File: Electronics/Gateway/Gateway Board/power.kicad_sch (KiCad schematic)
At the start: 25 parts, among them IC201 TPS54295PWPR, J2 Screw_Terminal_01x02, J202 Conn_01x02_Pin, J203 Conn_01x02_Pin, J204 Conn_01x02_Pin

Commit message: Schematic updates
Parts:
- removed C10, C11: 10n, Capacitor_SMD:C_0402_1005Metric, symbol Device:C_Small
- removed C3, C4: 100n, Capacitor_SMD:C_0402_1005Metric, symbol Device:C_Small
- removed C5: 1u, Capacitor_SMD:C_0402_1005Metric, symbol Device:C_Small
- removed C6, C7: 47u, Capacitor_SMD:C_0805_2012Metric, symbol Device:C_Small
- removed C8, C9: 10u, Capacitor_SMD:C_0603_1608Metric, symbol Device:C_Small
- removed D1: BAT760-115, Diode_SMD:D_SOD-323, symbol Device:D_Schottky
- removed D2, D3: Green, LED_SMD:LED_0603_1608Metric, symbol Device:LED_Small
- removed IC201: TPS54295PWPR, SOP65P640X120-17N, symbol TPS54295PWPR:TPS54295PWPR
- removed L1: 3u3, MSL Footprints:29332C, symbol Device:L_Small
- removed L2: 2u2, MSL Footprints:29222C, symbol Device:L_Small
- removed R1: 124k, Resistor_SMD:R_0402_1005Metric, symbol Device:R_Small
- removed R2: 22k1, Resistor_SMD:R_0402_1005Metric, symbol Device:R_Small
- removed R24: 2k2, Resistor_SMD:R_0402_1005Metric, symbol Device:R_Small
- removed R25: 1k5, Resistor_SMD:R_0402_1005Metric, symbol Device:R_Small
- removed R3: 33k, Resistor_SMD:R_0402_1005Metric, symbol Device:R_Small
- removed R4: 10k, Resistor_SMD:R_0402_1005Metric, symbol Device:R_Small
- added C201, C202, C207, C208, C209, C210: 22u, Capacitor_SMD:C_0603_1608Metric, symbol Device:C_Small
- added C203, C204, C205, C206: 100n, Capacitor_SMD:C_0402_1005Metric, symbol Device:C_Small
- added D202, D203: GREEN, LED_SMD:LED_0603_1608Metric, symbol Device:LED_Small
- added D204: ZMM10V, Diode_SMD:D_MiniMELF, symbol Diode:ZMMxx
- added IC201, IC202: TPS563202DRLR, MSL Footprints:SOTFL50P160X60-6N, symbol TPS563202DRLR:TPS563202DRLR
- added L201: 4u7, Inductor_SMD:L_Chilisin_BMRA00040420, symbol Device:L_Small
- added L202: 3u3, Inductor_SMD:L_Chilisin_BMRA00040420, symbol Device:L_Small
- added Q201: DMP3028LFDE, 101 Footprints:DMP2066UFDE7, symbol DMP3028LFDE-7:DMP3028LFDE
- added R201: 52k, Resistor_SMD:R_0402_1005Metric, symbol Device:R_Small
- added R202, R204: 10k, Resistor_SMD:R_0402_1005Metric, symbol Device:R_Small
- added R203: 31k, Resistor_SMD:R_0402_1005Metric, symbol Device:R_Small
- added R205: 2k2, Resistor_SMD:R_0402_1005Metric, symbol Device:R_Small
- added R206: 1k5, Resistor_SMD:R_0402_1005Metric, symbol Device:R_Small
- added R207: 330R, Resistor_SMD:R_0402_1005Metric, symbol Device:R_Small
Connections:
- net +5V: now also C207.1, C209.1, D202.2 (A), L201.2, R201.1
- net GND: now also C201.2, C202.2, C203.2, C204.2, C207.2, C208.2, C209.2, C210.2, IC201.3 (GND), IC202.3 (GND), R202.2, R204.2, R205.2, R206.2, R207.2
- net VIN: now also C201.1, C202.1, C203.1, C204.1, D204.1 (K), IC201.1 (VIN), IC201.5 (EN), IC202.1 (VIN), IC202.5 (EN), Q201.4 (S_1), Q201.7 (S_2)
- net VIN_RAW: now also Q201.1 (D_1), Q201.2 (D_2), Q201.5 (D_3), Q201.6 (D_4)
- new net +3.3V: C208.1, C210.1, D203.2 (A), L202.2, R203.1
- new net 3V3_BST: C206.1, IC202.4 (BST)
- new net 3V3_FB: IC202.6 (FB), R203.2, R204.1
- new net 3V3_LED_K: D203.1 (K), R206.1
- new net 3V3_SW: C206.2, IC202.2 (SW), L202.1
- new net 5V_BST: C205.1, IC201.4 (BST)
- new net 5V_FB: IC201.6 (FB), R201.2, R202.1
- new net 5V_LED_K: D202.1 (K), R205.1
- new net 5V_SW: C205.2, IC201.2 (SW), L201.1
- new net RP_PMOS_G: D204.2 (A), Q201.3 (G), R207.1
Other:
- note removed: "Max current: 2A per rail"
- moved on the sheet: J202, J203, J204

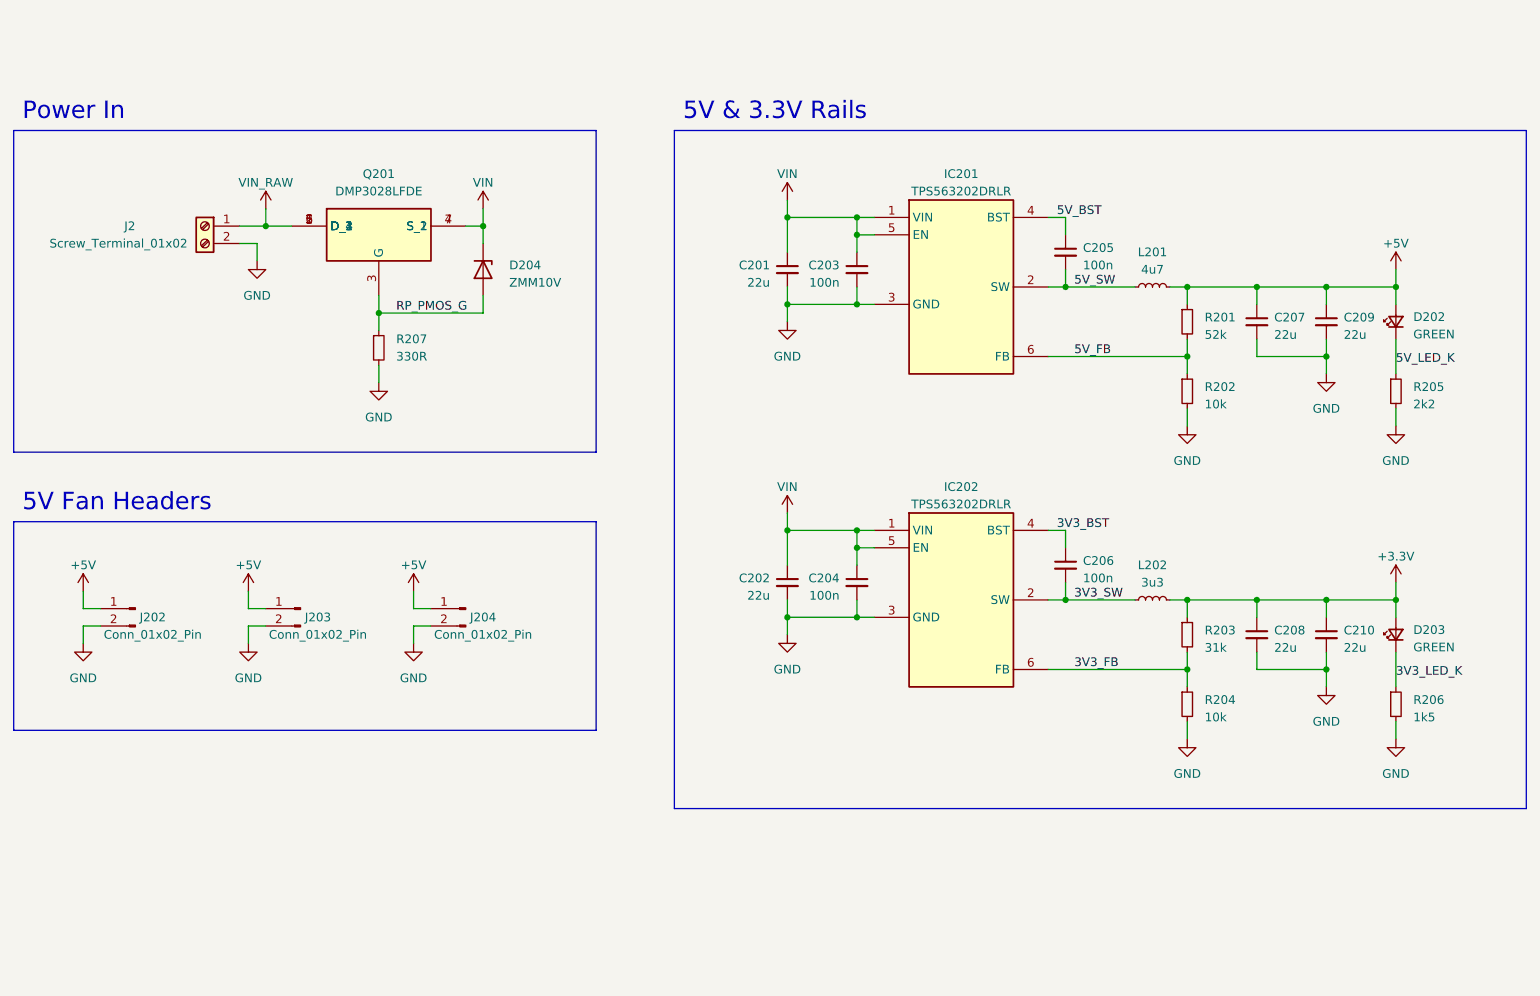
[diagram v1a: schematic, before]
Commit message: Gateway board layout complete and routing begun
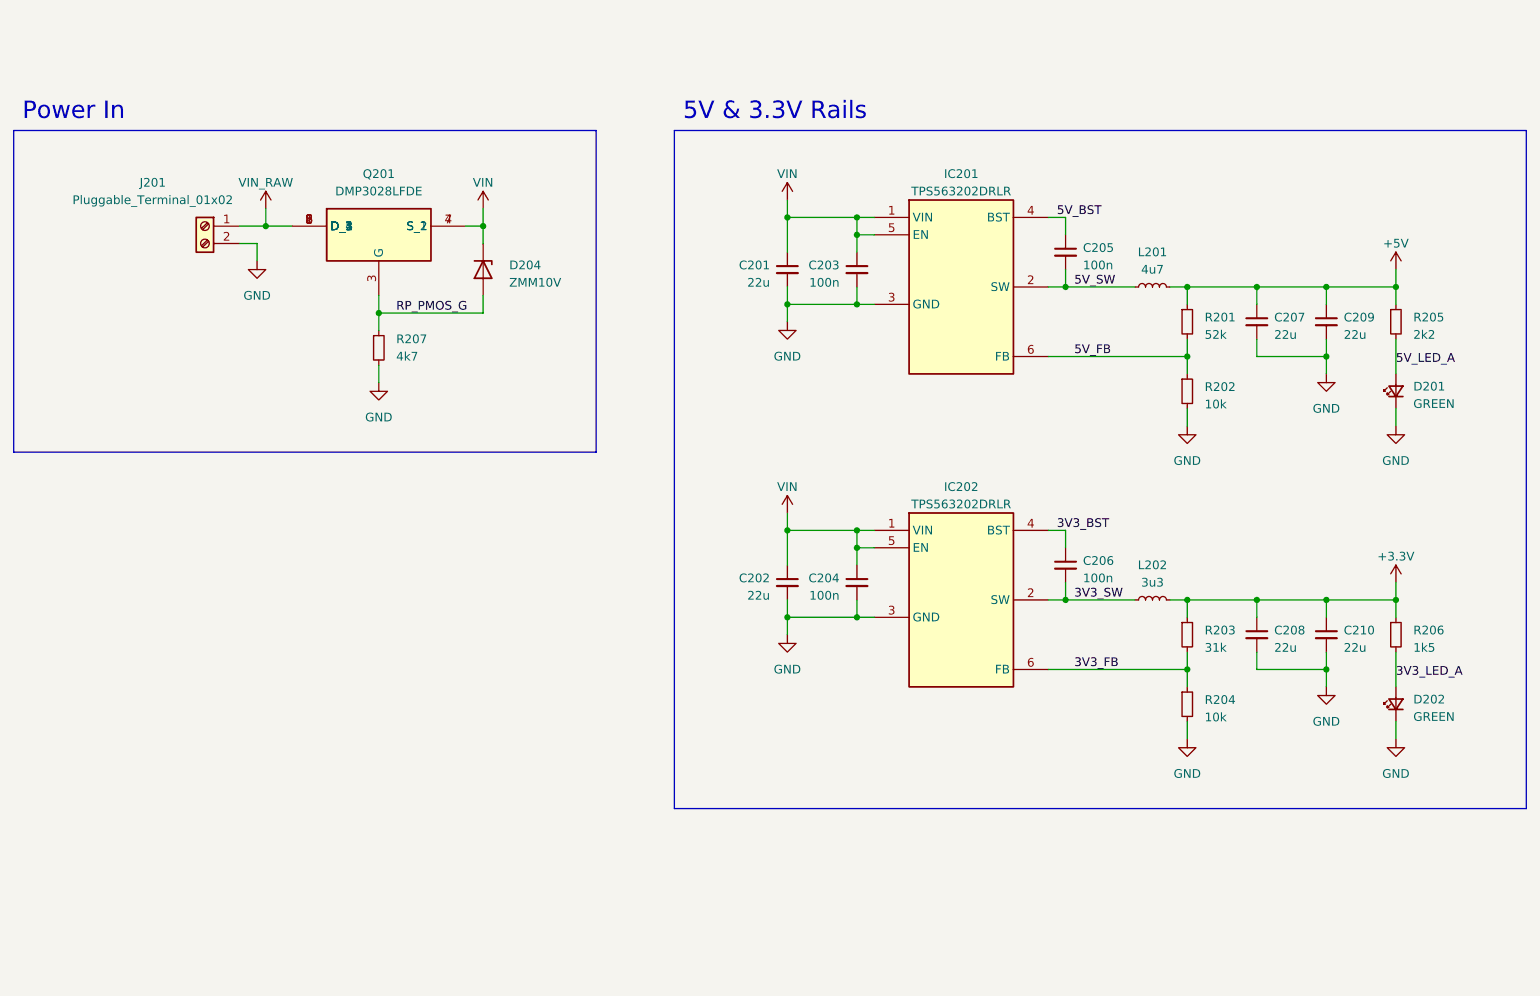
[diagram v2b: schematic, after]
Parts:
- removed D203: GREEN, LED_SMD:LED_0603_1608Metric, symbol Device:LED_Small
- removed J2: Screw_Terminal_01x02, TerminalBlock:TerminalBlock_bornier-2_P5.08mm, symbol Connector:Screw_Terminal_01x02
- removed J202, J203, J204: Conn_01x02_Pin, Connector_PinHeader_2.54mm:PinHeader_1x02_P2.54mm_Vertical, symbol Connector:Conn_01x02_Pin
- added D201: GREEN, LED_SMD:LED_0603_1608Metric, symbol Device:LED_Small
- added J201: Pluggable_Terminal_01x02, MSL Footprints:Pluggable_terminal-2_P5.08mm, symbol MSL_Symbols:Pluggable_Terminal_01x02
- Q201: footprint 101 Footprints:DMP2066UFDE7 -> MSL Footprints:DMP2066UFDE7
- R207: value 330R -> 4k7
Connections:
- net 3V3_LED_K is gone; now on net +3.3V: R206.1
- net +5V: now also R205.1; no longer D202.2 (A)
- net GND: now also D202.1 (K), D201.1 (K), J201.2 (Pin_2); no longer R205.2, R206.2
- net VIN_RAW: now also Q201.8 (D_5), J201.1 (Pin_1)
- removed net 5V_LED_K: D202.1 (K), R205.1
- new net 3V3_LED_A: D202.2 (A), R206.2
- new net 5V_LED_A: D201.2 (A), R205.2
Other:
- note removed: "5V Fan Headers"
